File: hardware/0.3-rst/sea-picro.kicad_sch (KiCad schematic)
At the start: 59 parts, among them J1 USB_C_Receptacle_USB2.0, J2 0.1" x 12, J3 0.1" x 12, J4 D+, J5 D-, Q1 2N7002VC-7, Q2 2N7002VC-7, SW1 SWITCH, U1 AP7365-33WG-7, U2 GD25Q64CWIGR, U3 RP2040, Y1 12MHz

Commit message: clean up routing
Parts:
- removed TP2: DELAY, josh-test-point:TestPoint_SMDPad_D1.0mm_NO_SILK, symbol Connector:TestPoint
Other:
- title: Sea Picro Reset -> Sea Picro RST
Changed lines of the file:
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@@
   (paper "A4")
   (title_block
-    (title "Sea Picro Reset")
-    (date "2022-03-13")
-    (rev "0.2")
+    (title "Sea Picro RST")
+    (date "2022-06-20")
+    (rev "0.3")
     (company "Josh Johnson")
   )
@@
   (junction (at 172.085 38.735) (diameter 0) (color 0 0 0 0)
   )
-  (junction (at 104.14 174.625) (diameter 0) (color 0 0 0 0)
-  )
   (junction (at 182.245 29.845) (diameter 0) (color 0 0 0 0)
   )
@@
     (stroke (width 0) (type default) (color 0 0 0 0))
   )
-  (wire (pts (xy 104.14 174.625) (xy 106.68 174.625))
+  (wire (pts (xy 101.6 174.625) (xy 106.68 174.625))
     (stroke (width 0) (type default) (color 0 0 0 0))
   )
@@
     (stroke (width 0) (type default) (color 0 0 0 0))
   )
-  (wire (pts (xy 101.6 174.625) (xy 104.14 174.625))
-    (stroke (width 0) (type default) (color 0 0 0 0))
-  )
   (wire (pts (xy 161.925 29.845) (xy 161.925 30.48))
     (stroke (width 0) (type default) (color 0 0 0 0))
@@
     )
   )
-  (symbol (lib_id "Connector:TestPoint") (at 104.14 174.625 0) (unit 1)
-    (in_bom no) (on_board yes)
-    (property "Reference" "TP2" (id 0) (at 101.6 167.64 0)
-      (effects (font (size 1.27 1.27)) (justify left))
-    )
-    (property "Value" "DELAY" (id 1) (at 101.6 169.545 0)
-      (effects (font (size 1.27 1.27)) (justify left))
-    )
-    (property "Footprint" "josh-test-point:TestPoint_SMDPad_D1.0mm_NO_SILK" (id 2) (at 109.22 174.625 0)
-      (effects (font (size 1.27 1.27)) hide)
-    )
-    (property "Datasheet" "~" (id 3) (at 109.22 174.625 0)
-      (effects (font (size 1.27 1.27)) hide)
-    )
-    (property "DNP" "DNP" (id 4) (at 104.14 174.625 0)
-      (effects (font (size 1.27 1.27)) hide)
-    )
-    (pin "1")
-  )
   (symbol (lib_id "Device:R") (at 161.29 93.345 90) (unit 1)
     (in_bom yes) (on_board yes)
@@
       (reference "TP1") (unit 1) (value "nRST") (footprint "josh-test-point:TestPoint_SMDPad_D1.0mm_NO_SILK")
     )
-    (path "/6932f11f-ad59-4756-a526-ea6bfbb8b520"
-      (reference "TP2") (unit 1) (value "DELAY") (footprint "josh-test-point:TestPoint_SMDPad_D1.0mm_NO_SILK")
-    )
     (path "/02975932-bf30-4606-900b-744ae844a718"

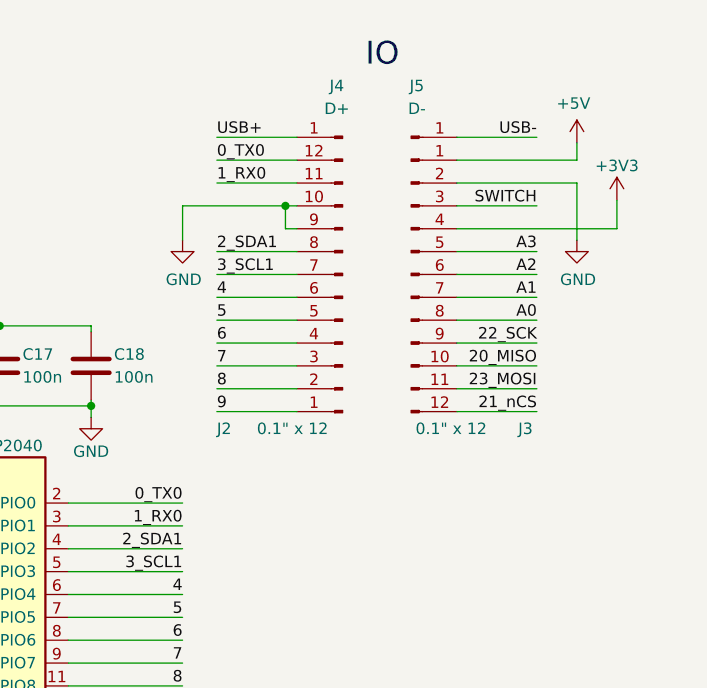
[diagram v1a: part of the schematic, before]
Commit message: rst moved to new footprints, clean up ext
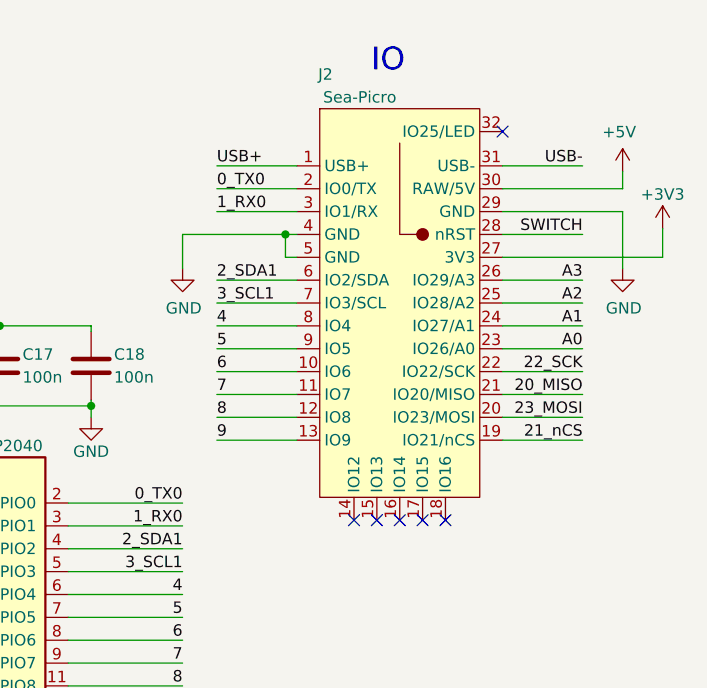
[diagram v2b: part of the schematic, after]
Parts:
- removed J2, J3: 0.1" x 12, josh-connectors:Castellated_Short_P2.54x12, symbol Connector:Conn_01x12_Male
- removed J4: D+, josh-connectors:PinHeader_1x01_P2.54mm_Circle, symbol Connector:Conn_01x01_Male
- removed J5: D-, josh-connectors:PinHeader_1x01_P2.54mm_Circle, symbol Connector:Conn_01x01_Male
- added J2: Sea-Picro, josh-module:Sea-Picro_RST_Pins, symbol josh-module:Sea-Picro
- D1: footprint Diode_SMD:D_SOD-323 -> josh-passives-smt:D_SOD-323
- Q1, Q2: footprint Package_TO_SOT_SMD:SOT-563 -> josh-soic-sot-etc:SOT-563
- U1: footprint Package_TO_SOT_SMD:SOT-23-5 -> josh-soic-sot-etc:SOT-23-5
- U2: footprint Package_SON:WSON-8-1EP_6x5mm_P1.27mm_EP3.4x4mm -> josh-dfn-qfn:WSON-8-1EP_6x5mm_P1.27mm_EP3.4x4mm
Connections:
- net +3V3: now also J2.27 (3V3)
- net +5V: now also J2.30 (RAW/5V)
- net 0_TX0: now also J2.2 (IO0/TX)
- net 1_RX0: now also J2.3 (IO1/RX)
- net 20_MISO: now also J2.21 (IO20/MISO)
- net 21_nCS: now also J2.19 (IO21/nCS)
- net 22_SCK: now also J2.22 (IO22/SCK)
- net 23_MOSI: now also J2.20 (IO23/MOSI)
- net 2_SDA1: now also J2.6 (IO2/SDA)
- net 3_SCL1: now also J2.7 (IO3/SCL)
- net 4: now also J2.8 (IO4)
- net 5: now also J2.9 (IO5)
- net 6: now also J2.10 (IO6)
- net 7: now also J2.11 (IO7)
- net 8: now also J2.12 (IO8)
- net 9: now also J2.13 (IO9)
- net A0: now also J2.23 (IO26/A0)
- net A1: now also J2.24 (IO27/A1)
- net A2: now also J2.25 (IO28/A2)
- net A3: now also J2.26 (IO29/A3)
- net GND: now also J2.29 (GND), J2.4 (GND), J2.5 (GND)
- net SWITCH: now also J2.28 (nRST)
- net USB+: now also J2.1 (USB+)
- net USB-: now also J2.31 (USB-)
- no-connect marks 11 -> 17

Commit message: update production outputs
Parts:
- C1, C10, C11, C12, C13, C14, C15, C16, C17, C18, C19, C2, C3, C4, C5, C6, C7, C8, C9, F1, J1, Q1, Q2, R1, R10, R11, R12, R13, R14, R15, R16, R17, R2, R3, R4, R5, R6, R7, R8, R9, SW1: Substitute (none) -> Y
- D1, D3, U3: Substitute (none) -> N
- D2: Substitute (none) -> Y - any pink
- J2: now left out of the parts list
- LOGO1, LOGO2, TP1, TP3, TP4, TP5: DNP DNP -> (none)
- U1: LCSC2 (none) -> C82942; MPN2 (none) -> ME6211C33M5G-N; Manufacturer2 (none) -> MICRONE(Nanjing Micro One Elec); Substitute (none) -> Y - Confirm with Josh
- U2: LCSC2 (none) -> C2940197; MPN2 (none) -> W25Q64JVZPIQ; Manufacturer2 (none) -> Winbond; Substitute (none) -> N
- Y1: LCSC2 (none) -> C2149205; MPN2 (none) -> 2TJ412000NYGBC; Manufacturer2 (none) -> JYJE; Substitute (none) -> N

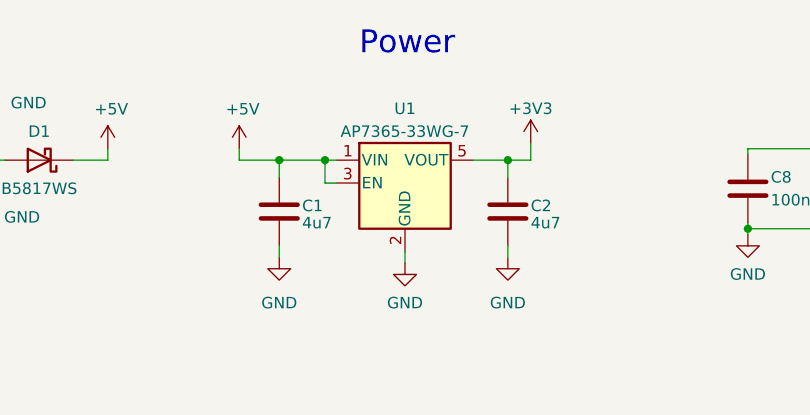
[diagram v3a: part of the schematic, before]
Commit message: add teardrops and melted versions, update LDO MPN
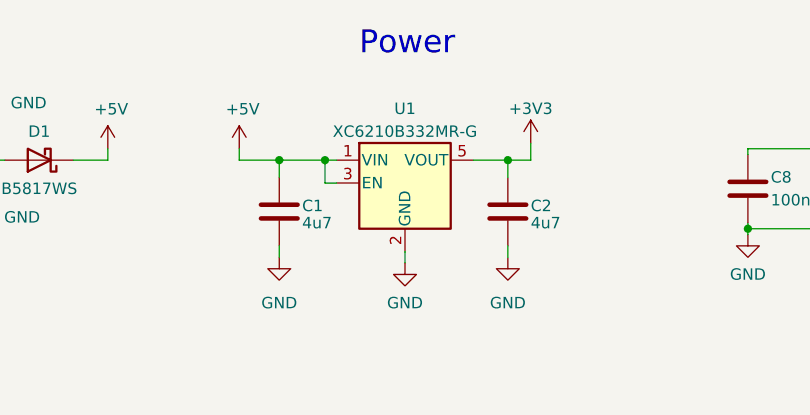
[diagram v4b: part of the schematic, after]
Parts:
- U1: value AP7365-33WG-7 -> XC6210B332MR-G; LCSC C150742 -> C47719; LCSC2 C82942 -> (none); MPN  AP7365-33WG-7 -> XC6210B332MR-G; MPN2 ME6211C33M5G-N -> (none); Manufacturer Diodes Incorporated -> Torex Semiconductor; Manufacturer2 MICRONE(Nanjing Micro One Elec) -> (none); Substitute Y - Confirm with Josh -> N
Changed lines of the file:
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@@
     (in_bom yes) (on_board yes)
     (property "Reference" "U1" (id 0) (at 113.665 25.4 0))
-    (property "Value" "AP7365-33WG-7 " (id 1) (at 113.665 27.94 0))
+    (property "Value" "XC6210B332MR-G" (id 1) (at 113.665 27.94 0))
     (property "Footprint" "josh-soic-sot-etc:SOT-23-5" (id 2) (at 113.665 25.4 0)
       (effects (font (size 1.27 1.27)) hide)
@@
       (effects (font (size 1.27 1.27)) hide)
     )
-    (property "LCSC" "C150742" (id 4) (at 113.665 33.655 0)
-      (effects (font (size 1.27 1.27)) hide)
-    )
-    (property "MPN " "AP7365-33WG-7 " (id 5) (at 113.665 33.655 0)
-      (effects (font (size 1.27 1.27)) hide)
-    )
-    (property "Manufacturer" "Diodes Incorporated" (id 6) (at 113.665 33.655 0)
+    (property "LCSC" "C47719" (id 4) (at 113.665 33.655 0)
+      (effects (font (size 1.27 1.27)) hide)
+    )
+    (property "MPN " "XC6210B332MR-G" (id 5) (at 113.665 33.655 0)
+      (effects (font (size 1.27 1.27)) hide)
+    )
+    (property "Manufacturer" "Torex Semiconductor" (id 6) (at 113.665 33.655 0)
       (effects (font (size 1.27 1.27)) hide)
     )
@@
       (effects (font (size 1.27 1.27)) hide)
     )
-    (property "LCSC2" "C82942" (id 8) (at 113.665 33.655 0)
-      (effects (font (size 1.27 1.27)) hide)
-    )
-    (property "MPN2" "ME6211C33M5G-N" (id 9) (at 113.665 33.655 0)
-      (effects (font (size 1.27 1.27)) hide)
-    )
-    (property "Manufacturer2" "MICRONE(Nanjing Micro One Elec) " (id 10) (at 113.665 33.655 0)
-      (effects (font (size 1.27 1.27)) hide)
-    )
-    (property "Substitute" "Y - Confirm with Josh" (id 11) (at 113.665 33.655 0)
+    (property "LCSC2" "" (id 8) (at 113.665 33.655 0)
+      (effects (font (size 1.27 1.27)) hide)
+    )
+    (property "MPN2" "" (id 9) (at 113.665 33.655 0)
+      (effects (font (size 1.27 1.27)) hide)
+    )
+    (property "Manufacturer2" "" (id 10) (at 113.665 33.655 0)
+      (effects (font (size 1.27 1.27)) hide)
+    )
+    (property "Substitute" "N" (id 11) (at 113.665 33.655 0)
       (effects (font (size 1.27 1.27)) hide)
     )
@@
     )
     (path "/d26fce45-c1d6-42bc-931d-972bf3799097"
-      (reference "U1") (unit 1) (value "AP7365-33WG-7 ") (footprint "josh-soic-sot-etc:SOT-23-5")
+      (reference "U1") (unit 1) (value "XC6210B332MR-G") (footprint "josh-soic-sot-etc:SOT-23-5")
     )
     (path "/578f7d98-6025-491f-b2c7-18b0b10fb26e"

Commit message: fix 1u cap bom
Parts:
- C12, C9: LCSC C15849 -> C52923; MPN  CL10A105KB8NNNC -> CL05A105KA5NQNC
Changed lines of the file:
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@@
       (effects (font (size 1.27 1.27)) hide)
     )
-    (property "LCSC" "C15849" (id 4) (at 159.385 76.2 0)
-      (effects (font (size 1.27 1.27)) hide)
-    )
-    (property "MPN " "CL10A105KB8NNNC" (id 5) (at 159.385 76.2 0)
+    (property "LCSC" "C52923" (id 4) (at 159.385 76.2 0)
+      (effects (font (size 1.27 1.27)) hide)
+    )
+    (property "MPN " "CL05A105KA5NQNC" (id 5) (at 159.385 76.2 0)
       (effects (font (size 1.27 1.27)) hide)
     )
@@
       (effects (font (size 1.27 1.27)) hide)
     )
-    (property "LCSC" "C15849" (id 4) (at 166.37 62.23 0)
-      (effects (font (size 1.27 1.27)) hide)
-    )
-    (property "MPN " "CL10A105KB8NNNC" (id 5) (at 166.37 62.23 0)
-      (effects (font (size 1.27 1.27)) hide)
-    )
+    (property "LCSC" "C52923" (id 4) (at 166.37 62.23 0)
+      (effects (font (size 1.27 1.27)) hide)
+    )
+    (property "MPN " "CL05A105KA5NQNC" (id 5) (at 166.37 62.23 0)
+      (effects (font (size 1.27 1.27)) hide)
+    )
